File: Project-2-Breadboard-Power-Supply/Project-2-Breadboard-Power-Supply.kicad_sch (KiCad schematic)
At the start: 0 parts

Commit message: setup and add symbols and library symbols
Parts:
- added C1, C2, C3: C, symbol Device:C
- added D1: LED, symbol Device:LED
- added J1, J2: Conn_01x02_Pin, symbol Connector:Conn_01x02_Pin
- added J3, J4: Conn_01x03_Pin, symbol Connector:Conn_01x03_Pin
- added J5: Screw_Terminal_01x02, symbol Connector:Screw_Terminal_01x02
- added J6: Barrel_Jack_Switch, symbol Connector:Barrel_Jack_Switch
- added R1, R2, R3: R, symbol Device:R
- added S1: EG1218, digikey-footprints:Switch_Slide_11.6x4mm_EG1218, symbol dk_Slide-Switches:EG1218
- added U1: LM7805_TO220, Package_TO_SOT_THT:TO-220-3_Vertical, symbol Regulator_Linear:LM7805_TO220
- added U2: LM317_TO-220, Package_TO_SOT_THT:TO-220-3_Vertical, symbol Regulator_Linear:LM317_TO-220

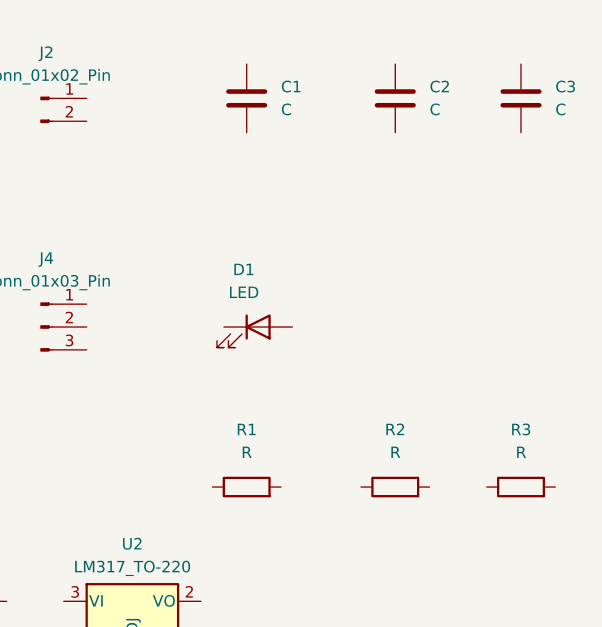
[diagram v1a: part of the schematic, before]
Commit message: set symbols' values for Resistors and Capacitors (part of step 2)
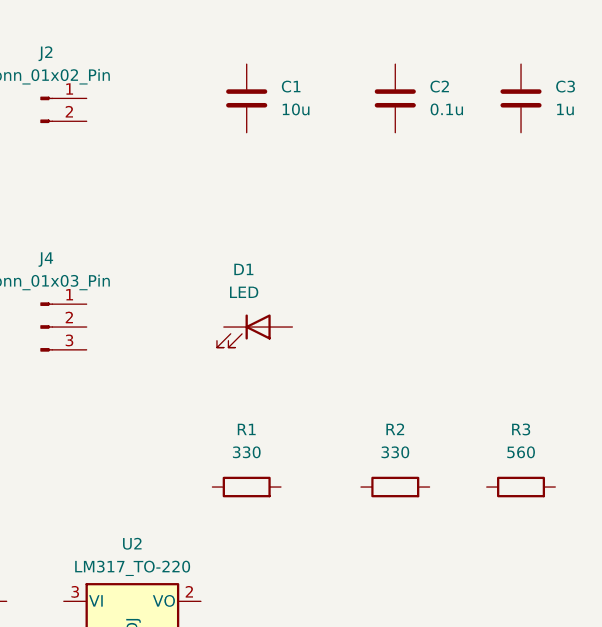
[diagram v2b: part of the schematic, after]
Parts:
- C1: value C -> 10u
- C2: value C -> 0.1u
- C3: value C -> 1u
- R1, R2: value R -> 330
- R3: value R -> 560
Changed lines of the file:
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@@
 			)
 		)
-		(property "Value" "R"
+		(property "Value" "560"
 			(at 161.29 88.9 90)
 			(show_name no)
@@
 			(at 161.29 92.71 0)
 			(hide yes)
+			(show_name no)
+			(do_not_autoplace no)
+			(effects
+				(font
+					(size 1.27 1.27)
+				)
+			)
+		)
+		(property "MPN" ""
+			(at 161.29 92.71 0)
+			(show_name no)
+			(do_not_autoplace no)
+			(effects
+				(font
+					(size 1.27 1.27)
+				)
+			)
+		)
+		(property "Manufacturer" ""
+			(at 161.29 92.71 0)
 			(show_name no)
 			(do_not_autoplace no)
@@
 			)
 		)
-		(property "Value" "C"
+		(property "Value" "10u"
 			(at 134.62 50.7999 0)
 			(show_name no)
@@
 			(at 130.81 49.53 0)
 			(hide yes)
+			(show_name no)
+			(do_not_autoplace no)
+			(effects
+				(font
+					(size 1.27 1.27)
+				)
+			)
+		)
+		(property "MPN" ""
+			(at 130.81 49.53 0)
+			(show_name no)
+			(do_not_autoplace no)
+			(effects
+				(font
+					(size 1.27 1.27)
+				)
+			)
+		)
+		(property "Manufacturer" ""
+			(at 130.81 49.53 0)
 			(show_name no)
 			(do_not_autoplace no)
@@
 			)
 		)
-		(property "Value" "R"
+		(property "Value" "330"
 			(at 130.81 88.9 90)
 			(show_name no)
@@
 			(at 130.81 92.71 0)
 			(hide yes)
+			(show_name no)
+			(do_not_autoplace no)
+			(effects
+				(font
+					(size 1.27 1.27)
+				)
+			)
+		)
+		(property "MPN" ""
+			(at 130.81 92.71 0)
+			(show_name no)
+			(do_not_autoplace no)
+			(effects
+				(font
+					(size 1.27 1.27)
+				)
+			)
+		)
+		(property "Manufacturer" ""
+			(at 130.81 92.71 0)
 			(show_name no)
 			(do_not_autoplace no)
@@
 			)
 		)
-		(property "Value" "R"
+		(property "Value" "330"
 			(at 147.32 88.9 90)
 			(show_name no)
@@
 			(at 147.32 92.71 0)
 			(hide yes)
+			(show_name no)
+			(do_not_autoplace no)
+			(effects
+				(font
+					(size 1.27 1.27)
+				)
+			)
+		)
+		(property "MPN" ""
+			(at 147.32 92.71 0)
+			(show_name no)
+			(do_not_autoplace no)
+			(effects
+				(font
+					(size 1.27 1.27)
+				)
+			)
+		)
+		(property "Manufacturer" ""
+			(at 147.32 92.71 0)
 			(show_name no)
 			(do_not_autoplace no)
@@
 			)
 		)
-		(property "Value" "C"
+		(property "Value" "0.1u"
 			(at 151.13 50.7999 0)
 			(show_name no)
@@
 			(at 147.32 49.53 0)
 			(hide yes)
+			(show_name no)
+			(do_not_autoplace no)
+			(effects
+				(font
+					(size 1.27 1.27)
+				)
+			)
+		)
+		(property "MPN" ""
+			(at 147.32 49.53 0)
+			(show_name no)
+			(do_not_autoplace no)
+			(effects
+				(font
+					(size 1.27 1.27)
+				)
+			)
+		)
+		(property "Manufacturer" ""
+			(at 147.32 49.53 0)
 			(show_name no)
 			(do_not_autoplace no)
@@
 			)
 		)
-		(property "Value" "C"
+		(property "Value" "1u"
 			(at 165.1 50.7999 0)
 			(show_name no)
@@
 			(show_name no)
 			(do_not_autoplace no)
+			(effects
+				(font
+					(size 1.27 1.27)
+				)
+			)
+		)
+		(property "MPN" ""
+			(at 161.29 49.53 0)
+			(show_name no)
+			(do_not_autoplace no)
+			(effects
+				(font
+					(size 1.27 1.27)
+				)
+			)
+		)
+		(property "Manufacturer" ""
+			(at 161.29 49.53 0)
+			(show_name no)
+			(do_not_autoplace no)

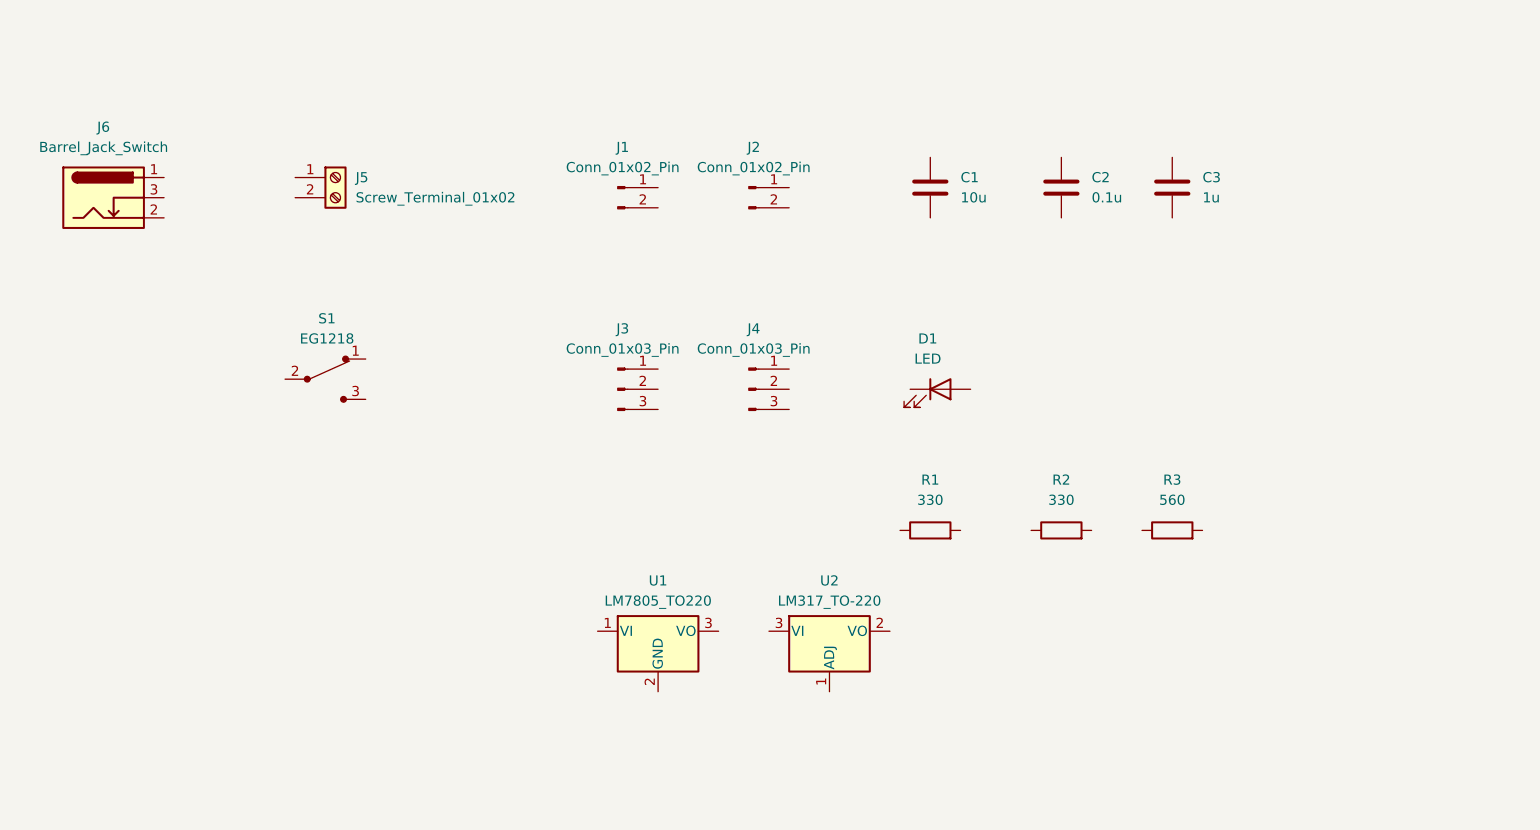
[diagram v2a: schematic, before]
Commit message: arrange symbols (step 2.1)
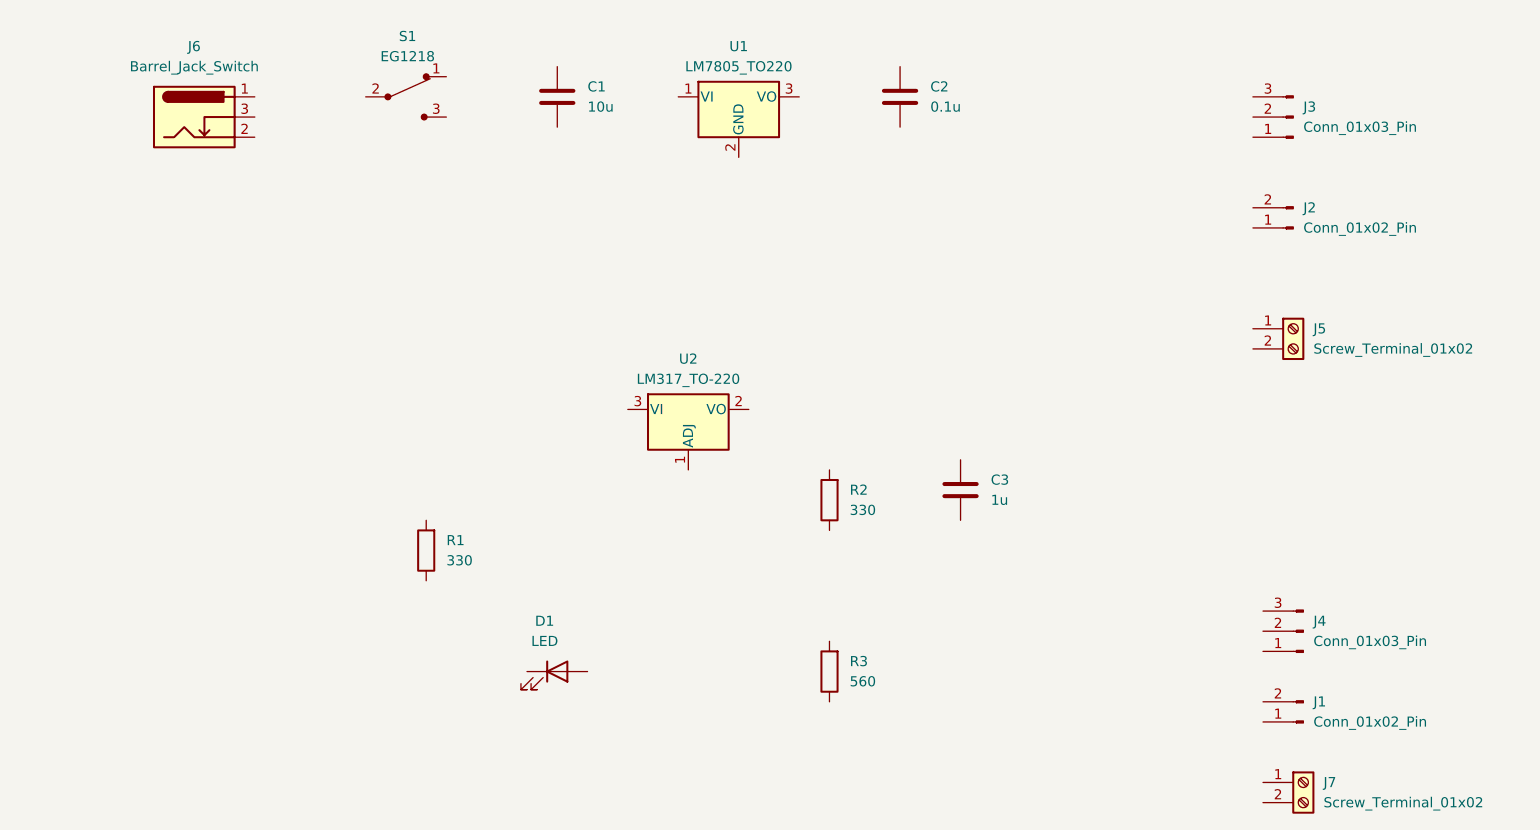
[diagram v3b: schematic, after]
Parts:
- added J7: Screw_Terminal_01x02, symbol Connector:Screw_Terminal_01x02
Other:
- moved on the sheet: C1, C2, C3, D1, J1, J2, J3, J4, J5, J6, R1, R2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

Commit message: add footprint associations (step 3.3)
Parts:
- C1, C2, C3: footprint (none) -> Capacitor_THT:C_Disc_D3.0mm_W1.6mm_P2.50mm
- D1: footprint (none) -> LED_THT:LED_D5.0mm
- J1, J2: footprint (none) -> Connector_PinHeader_2.54mm:PinHeader_1x02_P2.54mm_Vertical
- J3, J4: footprint (none) -> Connector_PinHeader_2.54mm:PinHeader_1x03_P2.54mm_Vertical
- J5, J7: footprint (none) -> TerminalBlock:TerminalBlock_bornier-2_P5.08mm
- J6: footprint (none) -> Connector_BarrelJack:BarrelJack_Horizontal
- R1, R2, R3: footprint (none) -> Resistor_THT:R_Axial_DIN0204_L3.6mm_D1.6mm_P7.62mm_Horizontal
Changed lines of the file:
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@@
 			)
 		)
-		(property "Footprint" ""
+		(property "Footprint" "Connector_PinHeader_2.54mm:PinHeader_1x03_P2.54mm_Vertical"
 			(at 177.8 105.41 0)
 			(hide yes)
@@
 			)
 		)
-		(property "Footprint" ""
+		(property "Footprint" "Resistor_THT:R_Axial_DIN0204_L3.6mm_D1.6mm_P7.62mm_Horizontal"
 			(at 119.888 110.49 90)
 			(hide yes)
@@
 			)
 		)
-		(property "Footprint" ""
+		(property "Footprint" "TerminalBlock:TerminalBlock_bornier-2_P5.08mm"
 			(at 177.8 124.46 0)
 			(hide yes)
@@
 			)
 		)
-		(property "Footprint" ""
+		(property "Footprint" "Capacitor_THT:C_Disc_D3.0mm_W1.6mm_P2.50mm"
 			(at 84.7852 41.91 0)
 			(hide yes)
@@
 			)
 		)
-		(property "Footprint" ""
+		(property "Footprint" "Connector_BarrelJack:BarrelJack_Horizontal"
 			(at 39.37 41.656 0)
 			(hide yes)
@@
 			(at 38.1 40.64 0)
 			(hide yes)
+			(show_name no)
+			(do_not_autoplace no)
+			(effects
+				(font
+					(size 1.27 1.27)
+				)
+			)
+		)
+		(property "MPN" ""
+			(at 38.1 40.64 0)
+			(show_name no)
+			(do_not_autoplace no)
+			(effects
+				(font
+					(size 1.27 1.27)
+				)
+			)
+		)
+		(property "Manufacturer" ""
+			(at 38.1 40.64 0)
 			(show_name no)
 			(do_not_autoplace no)
@@
 			)
 		)
-		(property "Footprint" ""
+		(property "Footprint" "Connector_PinHeader_2.54mm:PinHeader_1x02_P2.54mm_Vertical"
 			(at 176.53 54.61 0)
 			(hide yes)
@@
 			)
 		)
-		(property "Footprint" ""
+		(property "Footprint" "Connector_PinHeader_2.54mm:PinHeader_1x02_P2.54mm_Vertical"
 			(at 177.8 116.84 0)
 			(hide yes)
@@
 			)
 		)
-		(property "Footprint" ""
+		(property "Footprint" "Resistor_THT:R_Axial_DIN0204_L3.6mm_D1.6mm_P7.62mm_Horizontal"
 			(at 69.088 95.25 90)
 			(hide yes)
@@
 			)
 		)
-		(property "Footprint" ""
+		(property "Footprint" "Resistor_THT:R_Axial_DIN0204_L3.6mm_D1.6mm_P7.62mm_Horizontal"
 			(at 119.888 88.9 90)
 			(hide yes)
@@
 			)
 		)
-		(property "Footprint" ""
+		(property "Footprint" "Connector_PinHeader_2.54mm:PinHeader_1x03_P2.54mm_Vertical"
 			(at 176.53 40.64 0)
 			(hide yes)
@@
 			)
 		)
-		(property "Footprint" ""
+		(property "Footprint" "Capacitor_THT:C_Disc_D3.0mm_W1.6mm_P2.50mm"
 			(at 127.9652 41.91 0)
 			(hide yes)
@@
 			)
 		)
-		(property "Footprint" ""
+		(property "Footprint" "Capacitor_THT:C_Disc_D3.0mm_W1.6mm_P2.50mm"
 			(at 135.5852 91.44 0)
 			(hide yes)
@@
 			)
 		)
-		(property "Footprint" ""
+		(property "Footprint" "TerminalBlock:TerminalBlock_bornier-2_P5.08mm"
 			(at 176.53 67.31 0)
 			(hide yes)
@@
 			)
 		)
-		(property "Footprint" ""
+		(property "Footprint" "LED_THT:LED_D5.0mm"
 			(at 83.82 110.49 0)
 			(hide yes)

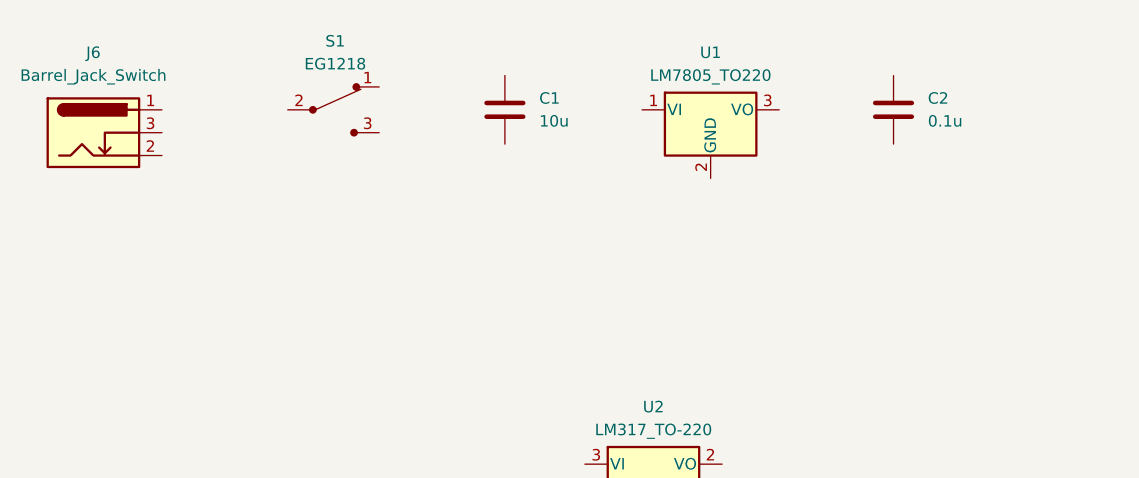
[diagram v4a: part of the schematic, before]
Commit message: add wiring (unfinished) (step 4)
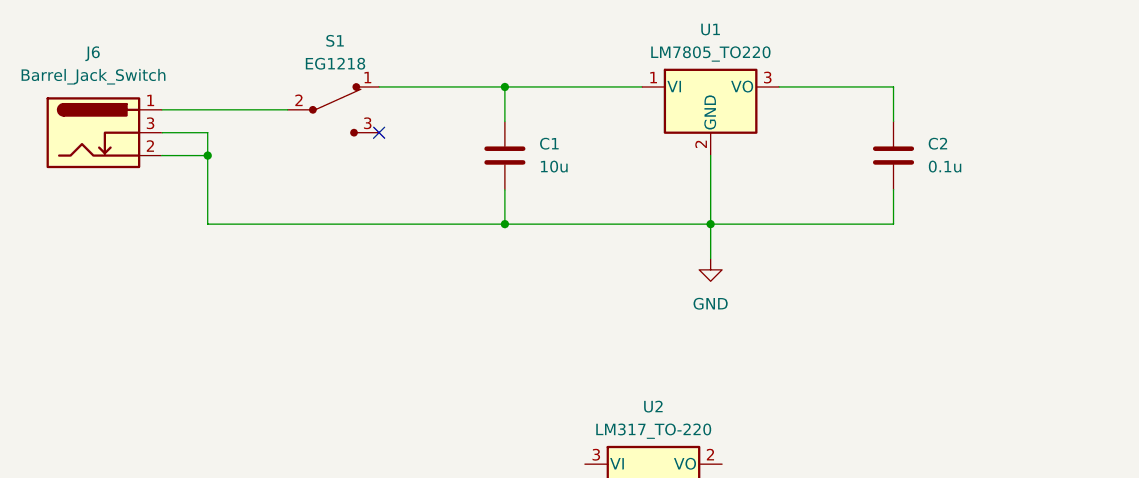
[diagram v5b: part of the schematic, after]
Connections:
- net at C1.1: now also S1.1, U1.1 (VI)
- net GND: now reaches C1.2
- net GND: now also C2.2, J6.2, J6.3, U1.2 (GND)
- net at S1.2: now also J6.1
- net at C2.1: now also U1.3 (VO)
- no-connect marks 0 -> 1
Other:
- moved on the sheet: C1, C2, U1
